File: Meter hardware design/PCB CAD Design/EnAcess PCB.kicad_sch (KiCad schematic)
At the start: 156 parts, among them J1 RTC, J10 curr, J11 , J12 RS232, J13 6v BAT, J14 Conn_01x01, J15 Conn_01x01, J16 Conn_01x01, J2 LCD pinout, J3 4x4 keypad, J4 Cicada GSM module, J5 , J6 , J7 relay, J8 220VAC.in, J9 LED_socket, Q1 BC547, Q2 BC547, Q3 IRF460, Q4 BC547, Q5 BC547, Q6 BC547, U1 UC3843_DIP8, U2 L7805, U3 PC817, U4 PC817, U5 LM350, U6 TL431LP, U7 LM350, U8 ATM90E26, U9 PC817

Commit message: PCB review (#8)
* Delete EnAcess PCB.kicad_sch-bak

* Delete Meter hardware design/PCB CAD Design directory

* Create CAD

* Add files via upload

* Delete Meter hardware design/production file directory

* Create pro

* Add files via upload
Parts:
- removed Q1, Q4, Q5, Q6: BC547, Package_TO_SOT_THT:TO-92_Inline_Wide, symbol Transistor_BJT:BC547
- removed R52: 470R, Resistor_THT:R_Axial_DIN0207_L6.3mm_D2.5mm_P10.16mm_Horizontal, symbol Device:R
- removed R53, R56, R57: 1K, Resistor_THT:R_Axial_DIN0207_L6.3mm_D2.5mm_P10.16mm_Horizontal, symbol Device:R
- removed U3, U9: PC817, Package_DIP:DIP-4_W7.62mm, symbol Isolator:PC817
- added C44: 104, Capacitor_THT:C_Disc_D10.0mm_W2.5mm_P5.00mm, symbol Device:C
- added D10, D13: 1n5819, Diode_THT:D_DO-34_SOD68_P7.62mm_Horizontal, symbol pspice:DIODE
- added D20, D9: D_Zener, Diode_THT:D_A-405_P12.70mm_Horizontal, symbol Device:D_Zener
- added J17: 6v BAT, Connector_JST:JST_EH_S2B-EH_1x02_P2.50mm_Horizontal, symbol Connector:Conn_01x02_Female
- added TR2: TRANSF3, Transformer_THT:Transformer_CHK_EI30-2VA_2xSec, symbol Transformer:TRANSF3
- added U10: L293, Package_DIP:DIP-16_W7.62mm, symbol Driver_Motor:L293
- D6: value 1n4007 -> 1n4148
- R11: value 1K -> 470R
- R4: value 470R -> 10R
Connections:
- net con A is gone; now on net +12V: R11.1
- net +5V: now also R4.1, D10.1 (K), D13.1 (K), D20.1 (K), D9.1 (K), U10.1 (EN1,2), U10.16 (VCC1); no longer C14.1, D2.2 (A), U2.3 (OUT)
- net 12V_S: now also U10.8 (VCC2)
- net GND: now also D20.2 (A), D9.2 (A), J17.2 (Pin_2), U10.12 (GND), U10.13 (GND), U10.4 (GND), U10.5 (GND)
- net REL_a: now also U10.7 (2A); no longer R4.1
- net REL_b: now also U10.2 (1A)
- net at J7.1 (Pin_1): now also C44.2, U10.3 (1Y)
- net at R11.2: now also R4.2, D10.2 (A), J17.1 (Pin_1)
- net at J7.2 (Pin_2): now also C44.1, U10.6 (2Y)
- new net: C14.1, D13.2 (A), D2.2 (A), U2.3 (OUT)
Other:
- note added: "."
- note added: "Feedback"
- note added: "Input"
- note added: "Output"
- note removed: "Magnetic latching relay control"
- moved on the sheet: J13, J7

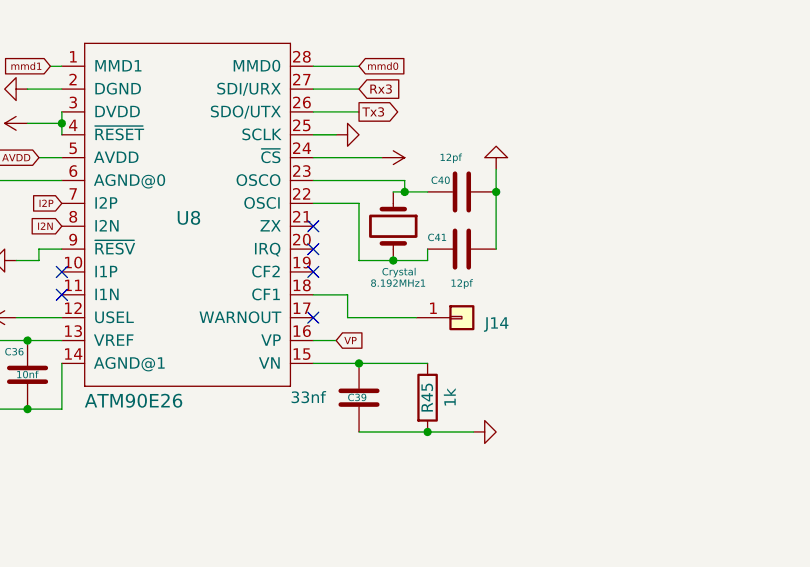
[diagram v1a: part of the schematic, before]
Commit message: Update malformed Crystal reference
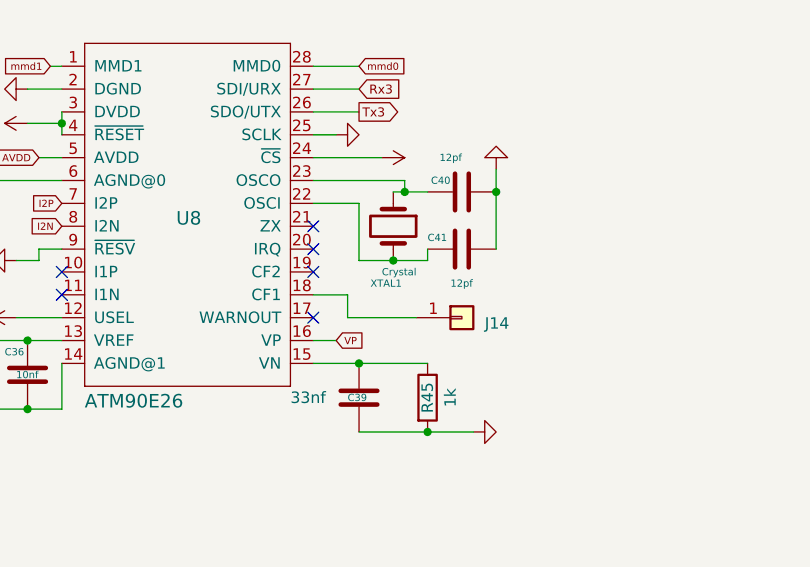
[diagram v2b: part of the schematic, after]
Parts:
- renumbered 8.192MHz1 to XTAL1
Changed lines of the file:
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@@
   (symbol (lib_id "Device:Crystal") (at 317.5 44.45 270) (unit 1)
     (in_bom yes) (on_board yes) (dnp no)
-    (property "Reference" "8.192MHz1" (at 314.96 50.8 90)
+    (property "Reference" "XTAL1" (at 314.96 50.8 90)
       (effects (font (size 0.8 0.8)) (justify left))
     )
@@
       (project "EnAcess PCB"
         (path "/e63e39d7-6ac0-4ffd-8aa3-1841a4541b55"
-          (reference "8.192MHz1") (unit 1)
+          (reference "XTAL1") (unit 1)
         )
       )
